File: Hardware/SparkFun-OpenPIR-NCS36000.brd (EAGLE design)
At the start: 27.9 x 35.6 mm, 35 parts, among them U1 NCS36000, U2 PIR

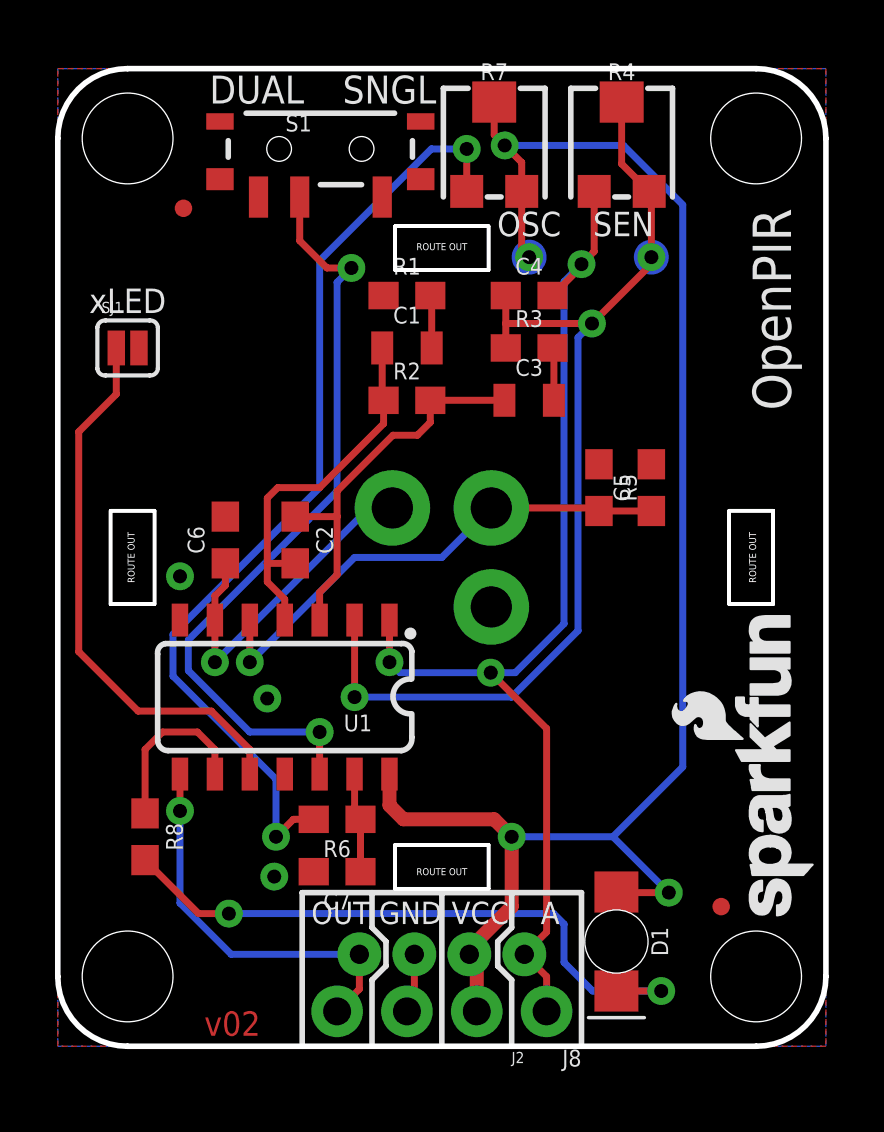
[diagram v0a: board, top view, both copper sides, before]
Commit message: Minor silkscreen adjustments. Incrementing to v10.
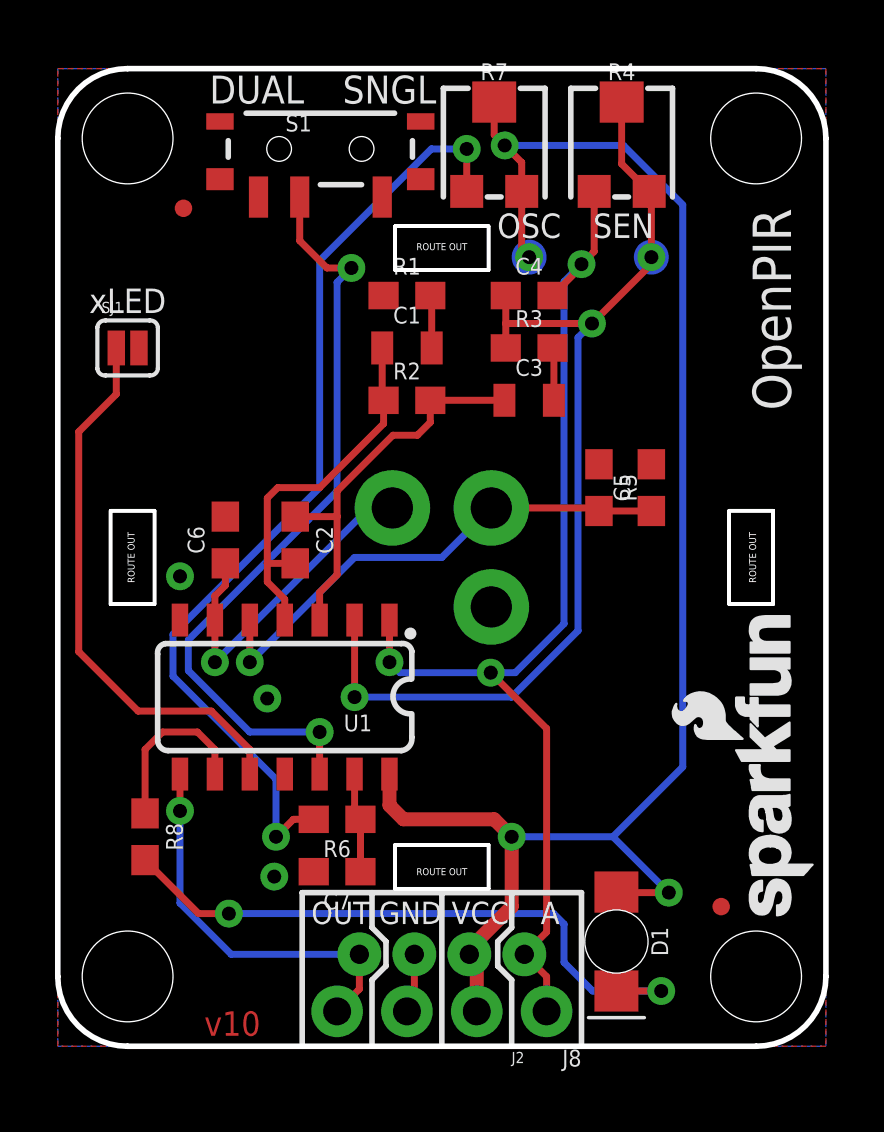
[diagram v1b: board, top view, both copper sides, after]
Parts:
- moved LOGO4 0.90 mm to (5.84, 32.6)
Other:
- board text added: "v10"
- board text removed: "v02"
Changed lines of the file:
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@@
 <setting verticaltext="up"/>
 </settings>
-<grid distance="0.05" unitdist="inch" unit="inch" style="lines" multiple="1" display="yes" altdistance="0.005" altunitdist="inch" altunit="inch"/>
+<grid distance="0.05" unitdist="inch" unit="inch" style="lines" multiple="1" display="yes" altdistance="0.0025" altunitdist="inch" altunit="inch"/>
 <layers>
 <layer number="1" name="Top" color="4" fill="1" visible="yes" active="yes"/>
@@
 <layer number="47" name="Measures" color="7" fill="1" visible="no" active="yes"/>
 <layer number="48" name="Document" color="7" fill="1" visible="no" active="yes"/>
-<layer number="49" name="Reference" color="7" fill="1" visible="yes" active="yes"/>
+<layer number="49" name="Reference" color="7" fill="1" visible="no" active="yes"/>
 <layer number="50" name="dxf" color="7" fill="1" visible="no" active="no"/>
 <layer number="51" name="tDocu" color="6" fill="1" visible="yes" active="yes"/>
@@
 <text x="7.239" y="34.29" size="1.016" layer="21" font="vector" ratio="15" align="bottom-center">DUAL</text>
 <text x="12.065" y="34.29" size="1.016" layer="21" font="vector" ratio="15" align="bottom-center">SNGL</text>
-<text x="17.145" y="30.353" size="0.889" layer="21" font="vector" ratio="15" align="top-center">OSC</text>
-<text x="20.574" y="30.353" size="0.889" layer="21" font="vector" ratio="15" align="top-center">SEN</text>
-<text x="13.97" y="32.004" size="1.524" layer="22" font="vector" ratio="15" rot="MR0" align="top-center">OpenPIR</text>
+<text x="17.145" y="30.2895" size="0.889" layer="21" font="vector" ratio="15" align="top-center">OSC</text>
+<text x="20.574" y="30.2895" size="0.889" layer="21" font="vector" ratio="15" align="top-center">SEN</text>
+<text x="13.97" y="32.131" size="1.524" layer="22" font="vector" ratio="15" rot="MR0" align="top-center">OpenPIR</text>
 <text x="26.67" y="30.48" size="1.397" layer="21" font="vector" ratio="15" rot="R90" align="bottom-right">OpenPIR</text>
 <text x="12.573" y="4.445" size="0.8128" layer="22" font="vector" ratio="15" rot="MR0" align="bottom-center">GND</text>
@@
 <dimension x1="0" y1="0" x2="10.16" y2="1.27" x3="-1.27" y3="0.635" textsize="0.889" textratio="15" layer="47" dtype="vertical" width="0.127" unit="inch" precision="3"/>
 <dimension x1="0" y1="0" x2="10.16" y2="1.27" x3="5.08" y3="-3.81" textsize="0.889" textratio="15" layer="47" dtype="horizontal" width="0.127" unit="inch" precision="3"/>
-<text x="6.35" y="0.381" size="0.889" layer="1" font="vector" ratio="15" align="bottom-center">v02</text>
+<text x="6.35" y="0.381" size="0.889" layer="1" font="vector" ratio="15" align="bottom-center">v10</text>
 <text x="21.59" y="-20.32" size="1.778" layer="51" font="vector" ratio="15">Jim Lindblom</text>
 <text x="21.717" y="3.937" size="1.016" layer="22" ratio="15" rot="MR90" align="bottom-center">DET</text>
@@
 <element name="LOGO1" library="SparkFun-Aesthetics" package="SFE_LOGO_NAME_FLAME_.1" value="SFE_LOGO_NAME_FLAME.1_INCH" x="27.559" y="4.318" rot="R90"/>
 <element name="LOGO3" library="SparkFun-Aesthetics" package="SFE_LOGO_NAME_.1" value="SFE_LOGO_NAME.1_INCH" x="22.987" y="31.877" rot="MR0"/>
-<element name="LOGO4" library="SparkFun-Aesthetics" package="OSHW-LOGO-S" value="OSHW-LOGOS" x="5.969" y="33.528" rot="MR0"/>
+<element name="LOGO4" library="SparkFun-Aesthetics" package="OSHW-LOGO-S" value="OSHW-LOGOS" x="5.842" y="32.639" rot="MR0"/>
 <element name="J8" library="SparkFun-Connectors" package="1X04_NO_SILK_ALL_ROUND" value="" x="17.78" y="1.27" rot="R180">
 <attribute name="PROD_ID" value="CONN-09696" x="17.78" y="1.27" size="1.016" layer="27" ratio="15" rot="R180" display="off"/>

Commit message: Fixing lens silkscreen, and moving r's, c's away from PIR sensor.
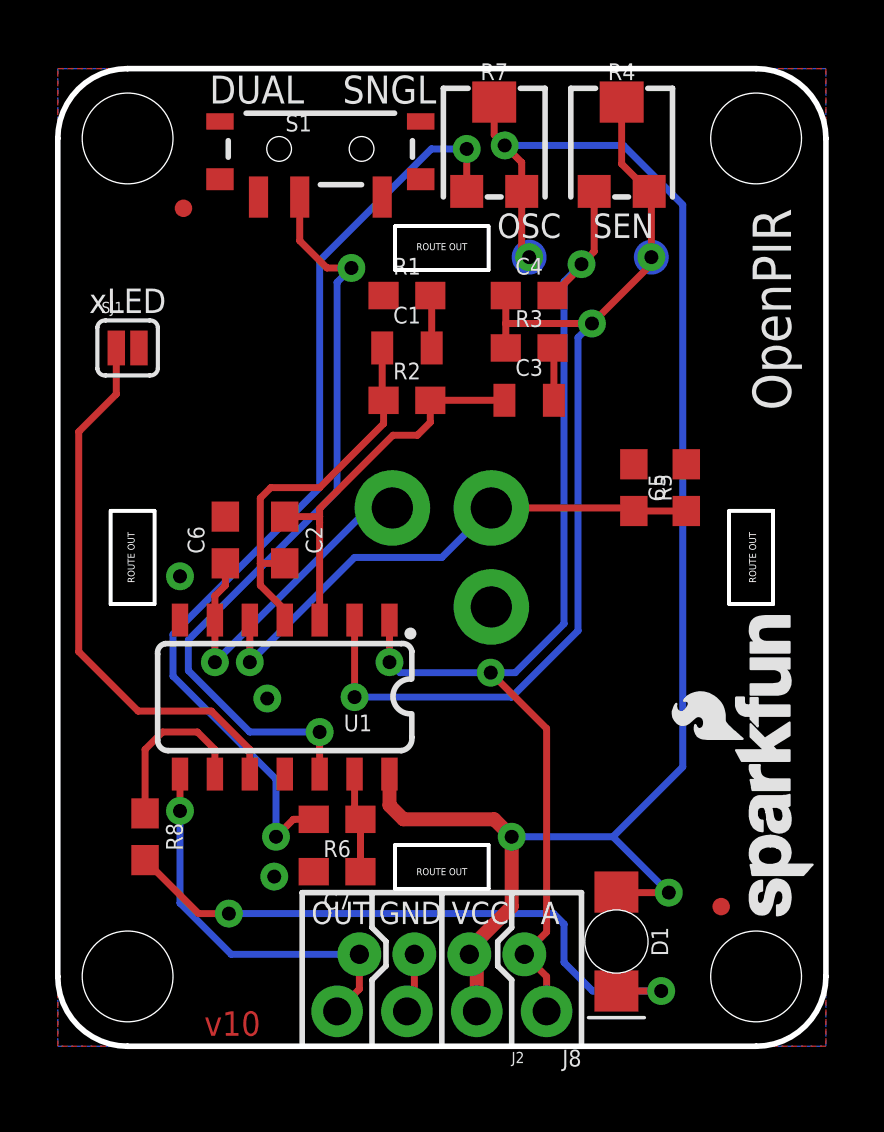
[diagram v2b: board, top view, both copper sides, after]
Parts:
- moved C5 1.27 mm to (22.9, 20.3)
- moved R5 1.27 mm to (21.0, 20.3)
- moved C2 0.38 mm to (8.26, 18.4)
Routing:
- net N$1: track 18.6 -> 19.8 mm
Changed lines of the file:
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@@
 <setting verticaltext="up"/>
 </settings>
-<grid distance="0.05" unitdist="inch" unit="inch" style="lines" multiple="1" display="yes" altdistance="0.0025" altunitdist="inch" altunit="inch"/>
+<grid distance="0.05" unitdist="inch" unit="inch" style="lines" multiple="1" display="yes" altdistance="0.005" altunitdist="inch" altunit="inch"/>
 <layers>
 <layer number="1" name="Top" color="4" fill="1" visible="yes" active="yes"/>
@@
 <layer number="47" name="Measures" color="7" fill="1" visible="no" active="yes"/>
 <layer number="48" name="Document" color="7" fill="1" visible="no" active="yes"/>
-<layer number="49" name="Reference" color="7" fill="1" visible="no" active="yes"/>
+<layer number="49" name="Reference" color="7" fill="1" visible="yes" active="yes"/>
 <layer number="50" name="dxf" color="7" fill="1" visible="no" active="no"/>
 <layer number="51" name="tDocu" color="6" fill="1" visible="yes" active="yes"/>
@@
 <attribute name="PROD_ID" value="IC-13432" x="8.255" y="12.7" size="1.778" layer="27" rot="R180" display="off"/>
 </element>
-<element name="R5" library="SparkFun-Resistors" package="0603" value="43k" x="19.685" y="20.32" rot="R270">
-<attribute name="VALUE" value="43k" x="19.685" y="20.32" size="1.778" layer="27" rot="R270" display="off"/>
-<attribute name="PROD_ID" value="RES-07858" x="19.685" y="20.32" size="1.778" layer="27" rot="R270" display="off"/>
+<element name="R5" library="SparkFun-Resistors" package="0603" value="43k" x="20.955" y="20.32" rot="R270">
+<attribute name="VALUE" value="43k" x="20.955" y="20.32" size="1.778" layer="27" rot="R270" display="off"/>
+<attribute name="PROD_ID" value="RES-07858" x="20.955" y="20.32" size="1.778" layer="27" rot="R270" display="off"/>
 </element>
 <element name="C6" library="SparkFun-Capacitors" package="0603" value="0.1uF" x="6.096" y="18.415" rot="R90">
 <attribute name="PROD_ID" value="CAP-00810" x="6.096" y="18.415" size="1.778" layer="27" font="vector" ratio="15" rot="R90" display="off"/>
 </element>
-<element name="C5" library="SparkFun-Capacitors" package="0603" value="0.1uF" x="21.59" y="20.32" rot="R90">
-<attribute name="PROD_ID" value="CAP-00810" x="21.59" y="20.32" size="1.778" layer="27" font="vector" ratio="15" rot="R90" display="off"/>
+<element name="C5" library="SparkFun-Capacitors" package="0603" value="0.1uF" x="22.86" y="20.32" rot="R90">
+<attribute name="PROD_ID" value="CAP-00810" x="22.86" y="20.32" size="1.778" layer="27" font="vector" ratio="15" rot="R90" display="off"/>
 </element>
 <element name="R1" library="SparkFun-Resistors" package="0603" value="10k" x="12.7" y="27.305">
@@
 <attribute name="PROD_ID" value="CAP-08402" x="12.7" y="25.4" size="1.778" layer="27" display="off"/>
 </element>
-<element name="C2" library="SparkFun-Capacitors" package="0603" value="10nF" x="8.636" y="18.415" rot="R270">
-<attribute name="PROD_ID" value="CAP-00867" x="8.636" y="18.415" size="1.778" layer="27" font="vector" ratio="15" rot="R270" display="off"/>
+<element name="C2" library="SparkFun-Capacitors" package="0603" value="10nF" x="8.255" y="18.415" rot="R270">
+<attribute name="PROD_ID" value="CAP-00867" x="8.255" y="18.415" size="1.778" layer="27" font="vector" ratio="15" rot="R270" display="off"/>
 </element>
 <element name="R2" library="openPIR-temp" package="0603" value="560k" x="12.7" y="23.495">
@@
 <wire x1="10.795" y1="17.78" x2="13.97" y2="17.78" width="0.254" layer="16"/>
 <wire x1="13.97" y1="17.78" x2="15.77" y2="19.58" width="0.254" layer="16"/>
-<wire x1="15.77" y1="19.58" x2="19.685" y2="19.58" width="0.254" layer="1"/>
-<wire x1="19.685" y1="19.58" x2="19.685" y2="19.47" width="0.254" layer="1"/>
-<wire x1="19.685" y1="19.47" x2="21.59" y2="19.47" width="0.254" layer="1"/>
+<wire x1="15.77" y1="19.58" x2="20.955" y2="19.58" width="0.254" layer="1"/>
+<wire x1="20.955" y1="19.58" x2="20.955" y2="19.47" width="0.254" layer="1"/>
+<wire x1="20.955" y1="19.47" x2="22.86" y2="19.47" width="0.254" layer="1"/>
 </signal>
 <signal name="VCC">
@@
 <contactref element="R2" pad="1"/>
 <contactref element="U1" pad="4"/>
-<wire x1="8.255" y1="15.5" x2="8.255" y2="16.256" width="0.254" layer="1"/>
-<wire x1="8.255" y1="16.256" x2="7.62" y2="16.891" width="0.254" layer="1"/>
-<wire x1="7.62" y1="17.565" x2="7.62" y2="19.939" width="0.254" layer="1"/>
-<wire x1="7.62" y1="19.939" x2="8.001" y2="20.32" width="0.254" layer="1"/>
-<wire x1="8.001" y1="20.32" x2="9.525" y2="20.32" width="0.254" layer="1"/>
+<wire x1="8.255" y1="15.5" x2="8.255" y2="15.875" width="0.254" layer="1"/>
+<wire x1="8.255" y1="15.875" x2="7.366" y2="16.764" width="0.254" layer="1"/>
+<wire x1="7.366" y1="17.565" x2="7.366" y2="19.939" width="0.254" layer="1"/>
+<wire x1="7.366" y1="19.939" x2="7.747" y2="20.32" width="0.254" layer="1"/>
+<wire x1="7.747" y1="20.32" x2="9.525" y2="20.32" width="0.254" layer="1"/>
 <wire x1="9.525" y1="20.32" x2="11.85" y2="22.645" width="0.254" layer="1"/>
 <wire x1="11.85" y1="22.645" x2="11.85" y2="23.495" width="0.254" layer="1"/>
-<wire x1="8.636" y1="17.565" x2="7.62" y2="17.565" width="0.254" layer="1"/>
-<wire x1="7.62" y1="17.565" x2="7.62" y2="16.891" width="0.254" layer="1"/>
+<wire x1="8.255" y1="17.565" x2="7.366" y2="17.565" width="0.254" layer="1"/>
+<wire x1="7.366" y1="17.565" x2="7.366" y2="16.764" width="0.254" layer="1"/>
 <wire x1="11.8" y1="25.4" x2="11.8" y2="23.545" width="0.254" layer="1"/>
 <wire x1="11.8" y1="23.545" x2="11.85" y2="23.495" width="0.254" layer="1"/>
@@
 <wire x1="13.081" y1="22.225" x2="13.55" y2="22.694" width="0.254" layer="1"/>
 <wire x1="13.55" y1="23.495" x2="13.55" y2="22.694" width="0.254" layer="1"/>
-<wire x1="9.525" y1="15.5" x2="9.525" y2="16.51" width="0.254" layer="1"/>
-<wire x1="9.525" y1="16.51" x2="10.16" y2="17.145" width="0.254" layer="1"/>
-<wire x1="10.16" y1="17.145" x2="10.16" y2="19.265" width="0.254" layer="1"/>
-<wire x1="10.16" y1="19.265" x2="10.16" y2="20.193" width="0.254" layer="1"/>
-<wire x1="10.16" y1="20.193" x2="12.192" y2="22.225" width="0.254" layer="1"/>
-<wire x1="8.636" y1="19.265" x2="10.16" y2="19.265" width="0.254" layer="1"/>
+<wire x1="9.525" y1="19.558" x2="12.192" y2="22.225" width="0.254" layer="1"/>
 <wire x1="16.245" y1="23.495" x2="13.55" y2="23.495" width="0.254" layer="1"/>
+<wire x1="9.525" y1="15.5" x2="9.525" y2="19.05" width="0.254" layer="1"/>
+<wire x1="9.525" y1="19.265" x2="9.525" y2="19.558" width="0.254" layer="1"/>
+<wire x1="8.255" y1="19.265" x2="9.525" y2="19.265" width="0.254" layer="1"/>
+<wire x1="9.525" y1="19.265" x2="9.525" y2="19.05" width="0.254" layer="1"/>
 </signal>
 <signal name="N$7">

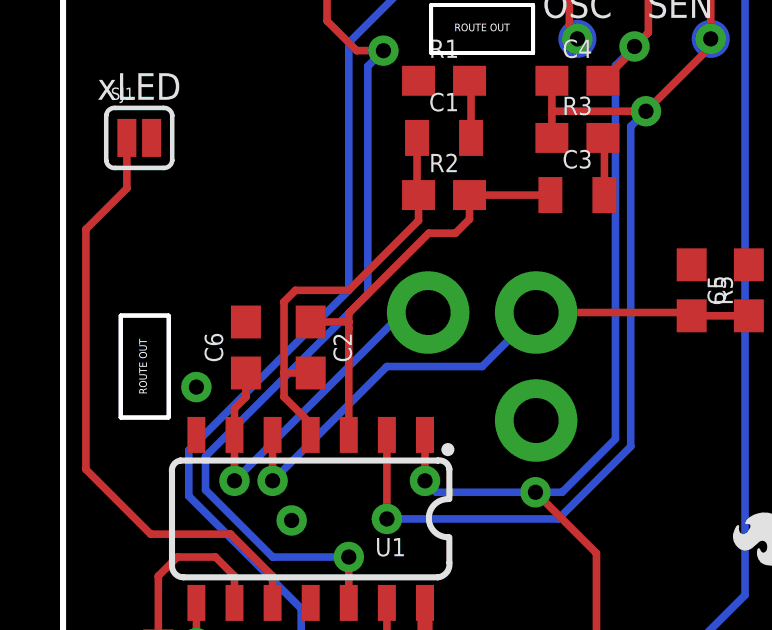
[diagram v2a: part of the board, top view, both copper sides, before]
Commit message: Moving C6 a bit, minor re-routing.
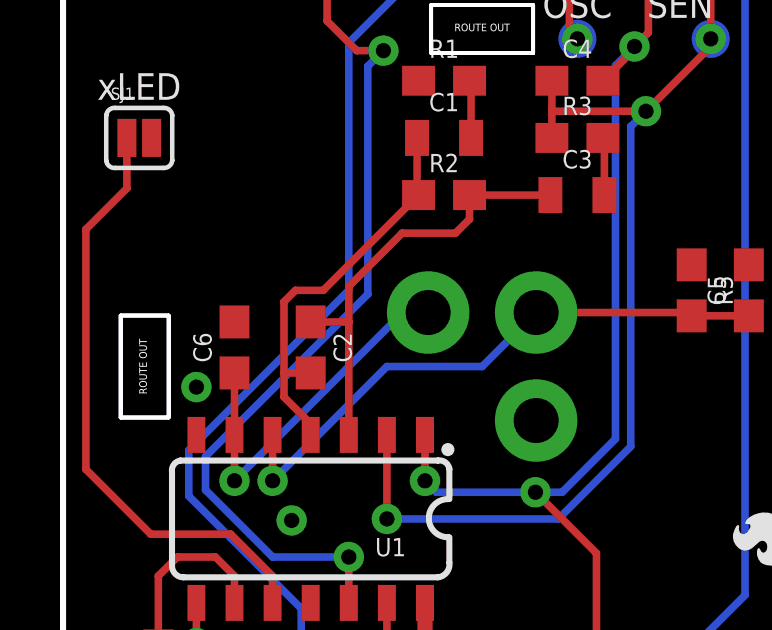
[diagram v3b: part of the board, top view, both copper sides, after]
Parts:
- moved C6 0.38 mm to (5.71, 18.4)
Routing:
- net N$6: track 14.1 -> 14.7 mm
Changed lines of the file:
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@@
 <layer number="47" name="Measures" color="7" fill="1" visible="no" active="yes"/>
 <layer number="48" name="Document" color="7" fill="1" visible="no" active="yes"/>
-<layer number="49" name="Reference" color="7" fill="1" visible="yes" active="yes"/>
+<layer number="49" name="Reference" color="7" fill="1" visible="no" active="yes"/>
 <layer number="50" name="dxf" color="7" fill="1" visible="no" active="no"/>
 <layer number="51" name="tDocu" color="6" fill="1" visible="yes" active="yes"/>
@@
 <attribute name="PROD_ID" value="RES-07858" x="20.955" y="20.32" size="1.778" layer="27" rot="R270" display="off"/>
 </element>
-<element name="C6" library="SparkFun-Capacitors" package="0603" value="0.1uF" x="6.096" y="18.415" rot="R90">
-<attribute name="PROD_ID" value="CAP-00810" x="6.096" y="18.415" size="1.778" layer="27" font="vector" ratio="15" rot="R90" display="off"/>
+<element name="C6" library="SparkFun-Capacitors" package="0603" value="0.1uF" x="5.715" y="18.415" rot="R90">
+<attribute name="PROD_ID" value="CAP-00810" x="5.715" y="18.415" size="1.778" layer="27" font="vector" ratio="15" rot="R90" display="off"/>
 </element>
 <element name="C5" library="SparkFun-Capacitors" package="0603" value="0.1uF" x="22.86" y="20.32" rot="R90">
@@
 <wire x1="5.715" y1="13.97" x2="11.325" y2="19.58" width="0.254" layer="16"/>
 <wire x1="11.325" y1="19.58" x2="12.17" y2="19.58" width="0.254" layer="16"/>
-<wire x1="5.715" y1="15.5" x2="5.715" y2="16.383" width="0.254" layer="1"/>
-<wire x1="5.715" y1="16.383" x2="6.096" y2="16.764" width="0.254" layer="1"/>
-<wire x1="6.096" y1="16.764" x2="6.096" y2="17.565" width="0.254" layer="1"/>
+<wire x1="5.715" y1="15.5" x2="5.715" y2="17.565" width="0.254" layer="1"/>
 </signal>
 <signal name="N$1">
@@
 <wire x1="7.366" y1="17.565" x2="7.366" y2="19.939" width="0.254" layer="1"/>
 <wire x1="7.366" y1="19.939" x2="7.747" y2="20.32" width="0.254" layer="1"/>
-<wire x1="7.747" y1="20.32" x2="9.525" y2="20.32" width="0.254" layer="1"/>
-<wire x1="9.525" y1="20.32" x2="11.85" y2="22.645" width="0.254" layer="1"/>
-<wire x1="11.85" y1="22.645" x2="11.85" y2="23.495" width="0.254" layer="1"/>
 <wire x1="8.255" y1="17.565" x2="7.366" y2="17.565" width="0.254" layer="1"/>
 <wire x1="7.366" y1="17.565" x2="7.366" y2="16.764" width="0.254" layer="1"/>
 <wire x1="11.8" y1="25.4" x2="11.8" y2="23.545" width="0.254" layer="1"/>
 <wire x1="11.8" y1="23.545" x2="11.85" y2="23.495" width="0.254" layer="1"/>
+<wire x1="7.747" y1="20.32" x2="8.675" y2="20.32" width="0.254" layer="1"/>
+<wire x1="8.675" y1="20.32" x2="11.85" y2="23.495" width="0.254" layer="1"/>
 </signal>
 <signal name="N$6">
@@
 <contactref element="U1" pad="3"/>
 <contactref element="C3" pad="1"/>
-<wire x1="12.192" y1="22.225" x2="13.081" y2="22.225" width="0.254" layer="1"/>
 <wire x1="13.081" y1="22.225" x2="13.55" y2="22.694" width="0.254" layer="1"/>
 <wire x1="13.55" y1="23.495" x2="13.55" y2="22.694" width="0.254" layer="1"/>
-<wire x1="9.525" y1="19.558" x2="12.192" y2="22.225" width="0.254" layer="1"/>
 <wire x1="16.245" y1="23.495" x2="13.55" y2="23.495" width="0.254" layer="1"/>
-<wire x1="9.525" y1="15.5" x2="9.525" y2="19.05" width="0.254" layer="1"/>
-<wire x1="9.525" y1="19.265" x2="9.525" y2="19.558" width="0.254" layer="1"/>
+<wire x1="9.525" y1="15.5" x2="9.525" y2="19.265" width="0.254" layer="1"/>
 <wire x1="8.255" y1="19.265" x2="9.525" y2="19.265" width="0.254" layer="1"/>
-<wire x1="9.525" y1="19.265" x2="9.525" y2="19.05" width="0.254" layer="1"/>
+<wire x1="9.525" y1="19.265" x2="9.525" y2="20.447" width="0.254" layer="1"/>
+<wire x1="9.525" y1="20.447" x2="11.303" y2="22.225" width="0.254" layer="1"/>
+<wire x1="11.303" y1="22.225" x2="13.081" y2="22.225" width="0.254" layer="1"/>
 </signal>
 <signal name="N$7">
